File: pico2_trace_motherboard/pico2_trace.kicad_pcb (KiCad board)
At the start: 2 copper layers, 92 x 64 mm, 56 parts, among them J10 SWD, J1B BREAKOUT, J2B BREAKOUT, J3 MIPI-20, J5 USB-A HOST, J6 CORTEX-10, J7 JST-SH-3 DEBUG_PROBE, J8 USB-MICROB PWR, J9 USB-MICROB DEV, SW1 RESET

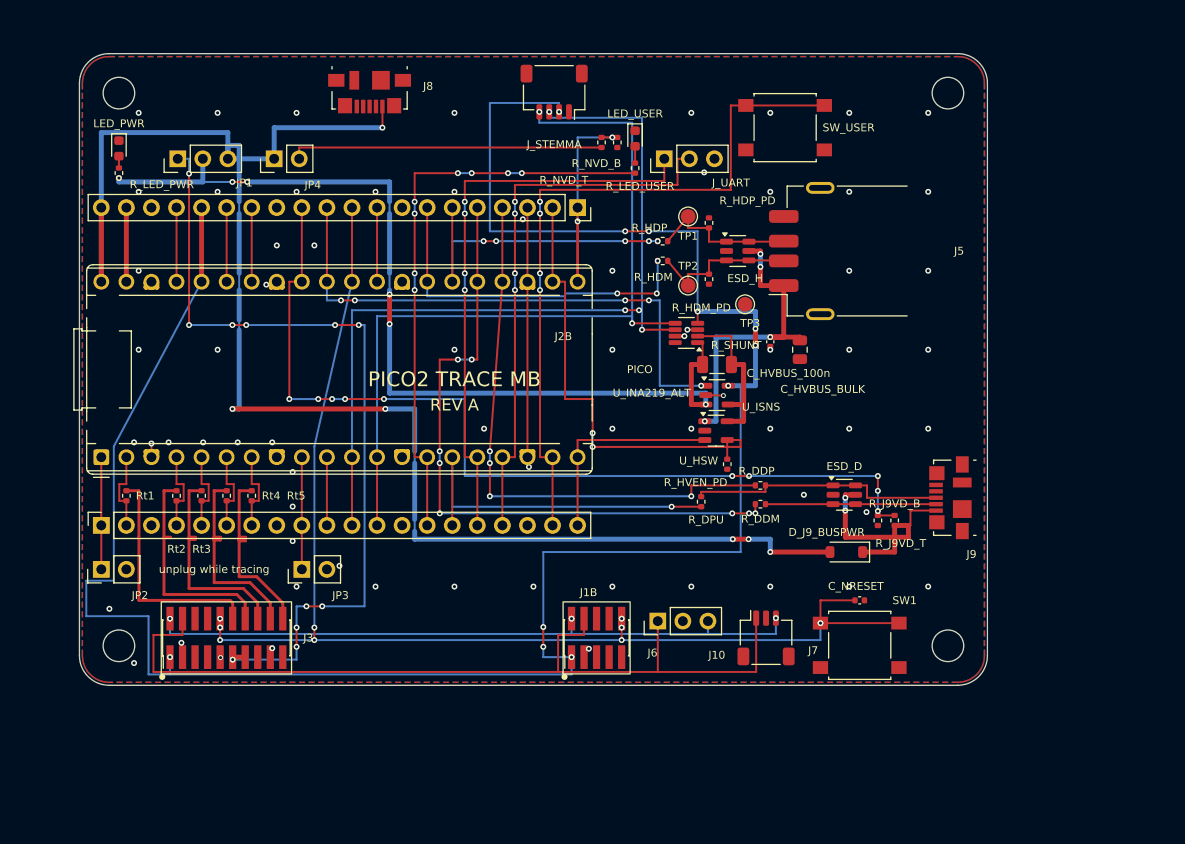
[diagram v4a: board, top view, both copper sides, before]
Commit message: pcb: DFM + pre-fab review fixes; fab package + BRINGUP
Via sizes, silkscreen legend, refdes/label clamping; diode direction
fix, J5 shell ground, VSYS diode-OR feed + decoupling, V5_JTRACE
widening; V2 trace-rate claim corrected; gerbers/BOM regenerated.
Squash of 93dd81b, 978ebdd, 41a4014, 6d67559, 0d99a43. Board copper
frozen here (= original 6d67559 geometry).
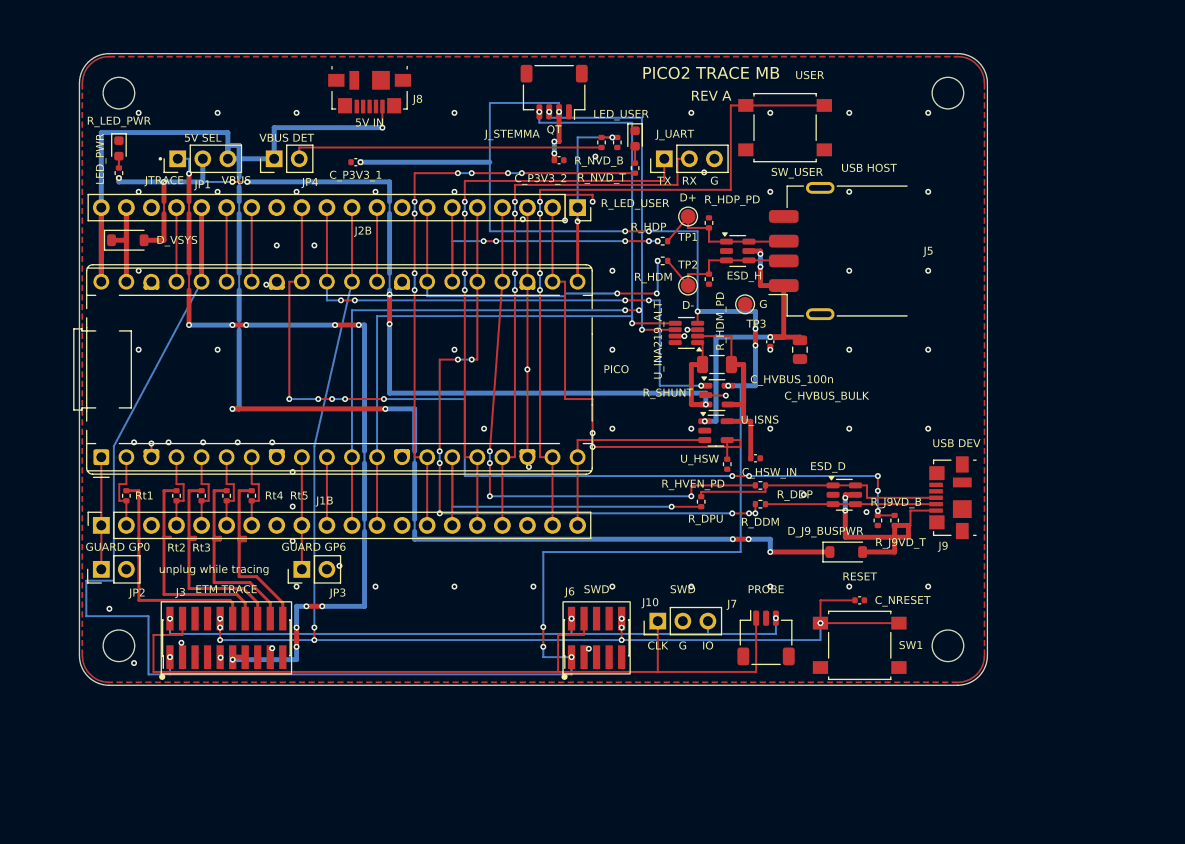
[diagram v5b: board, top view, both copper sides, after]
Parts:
- added C_HSW_IN: 100n/16V, C_0402_1005Metric, F.Cu at (68.5, 41.0)
- added C_P3V3_1: 100n/16V, C_0402_1005Metric, F.Cu at (28.0, 11.0)
- added C_P3V3_2: 100n/16V, C_0402_1005Metric, F.Cu at (48.6, 10.8)
- added D_VSYS: B5819W, D_SOD-123, F.Cu at (4.90, 18.9)
- turned D_J9_BUSPWR to 0 degrees
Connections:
- D_J9_BUSPWR pad 1: J9_VBUS -> VBUS_NET
- D_J9_BUSPWR pad 2: VBUS_NET -> J9_VBUS
- J5 pad 5: (no net) -> GND
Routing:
- net P3V3: track 224.0 -> 242.5 mm, vias 11 -> 14
- net VBUS_SEL: track 94.1 -> 102.0 mm, vias 6 -> 7
- net GND: track 30.5 -> 36.9 mm, vias 69 -> 73
- net VSYS: track 7.51 -> 12.3 mm
- net HOST_5V_IN: track 20.6 -> 25.0 mm
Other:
- board text added: "5V IN"
- board text added: "5V SEL"
- board text added: "CLK"
- board text added: "D+"
- board text added: "D-"
- board text added: "ETM TRACE"
- board text added: "G"
- board text added: "GUARD GP0"
- board text added: "GUARD GP6"
- board text added: "IO"
- board text added: "JTRACE"
- board text added: "PROBE"
- board text added: "QT"
- board text added: "RESET"
- board text added: "RX"
- board text added: "SWD"
- board text added: "TX"
- board text added: "USB DEV"
- board text added: "USB HOST"
- board text added: "USER"
- board text added: "VBUS"
- board text added: "VBUS DET"
